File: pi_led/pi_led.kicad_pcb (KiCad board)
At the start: 2 copper layers, 50 x 50 mm, 12 parts, among them CON1 PWR, P1 LED_STRIP, P2 RiPi, Q1 STP16NF06L, Q2 STP16NF06L, Q3 STP16NF06L

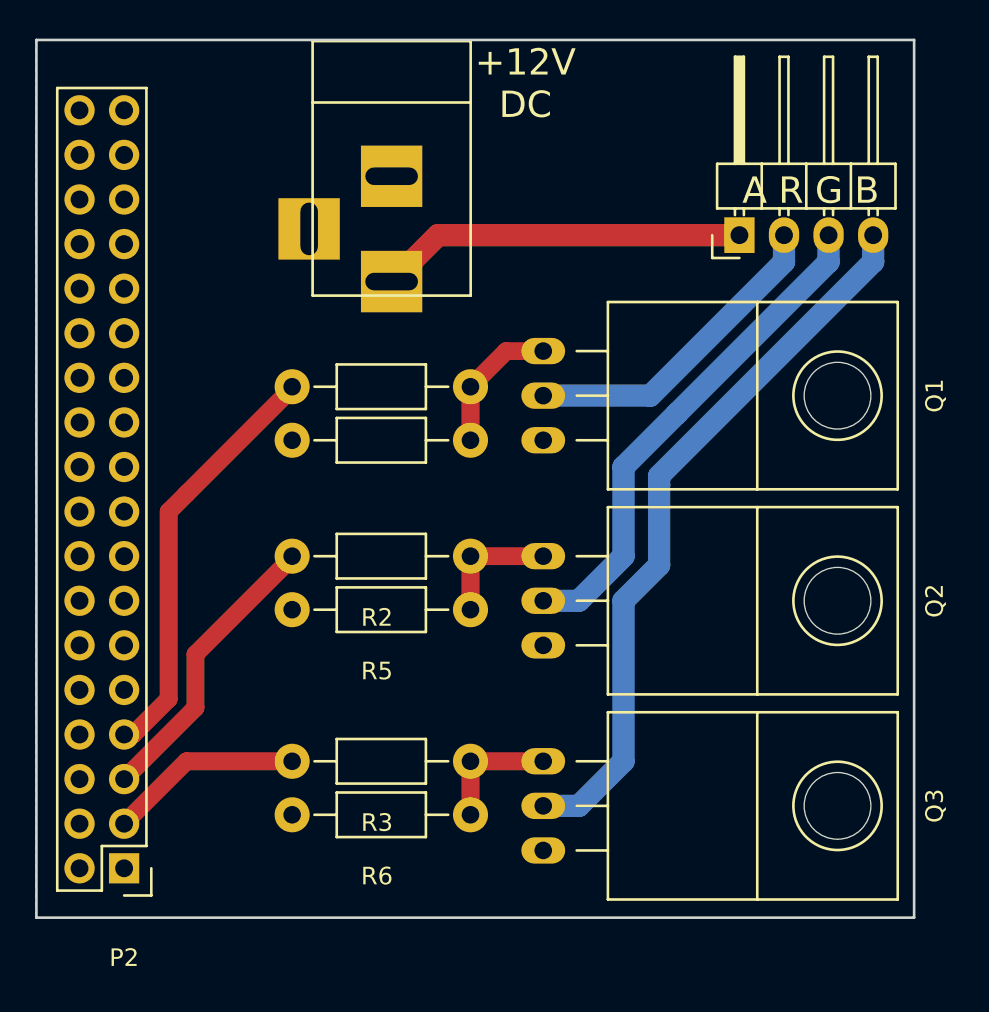
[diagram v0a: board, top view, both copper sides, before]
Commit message: Fix #2, Move labels to silk, General Tidying
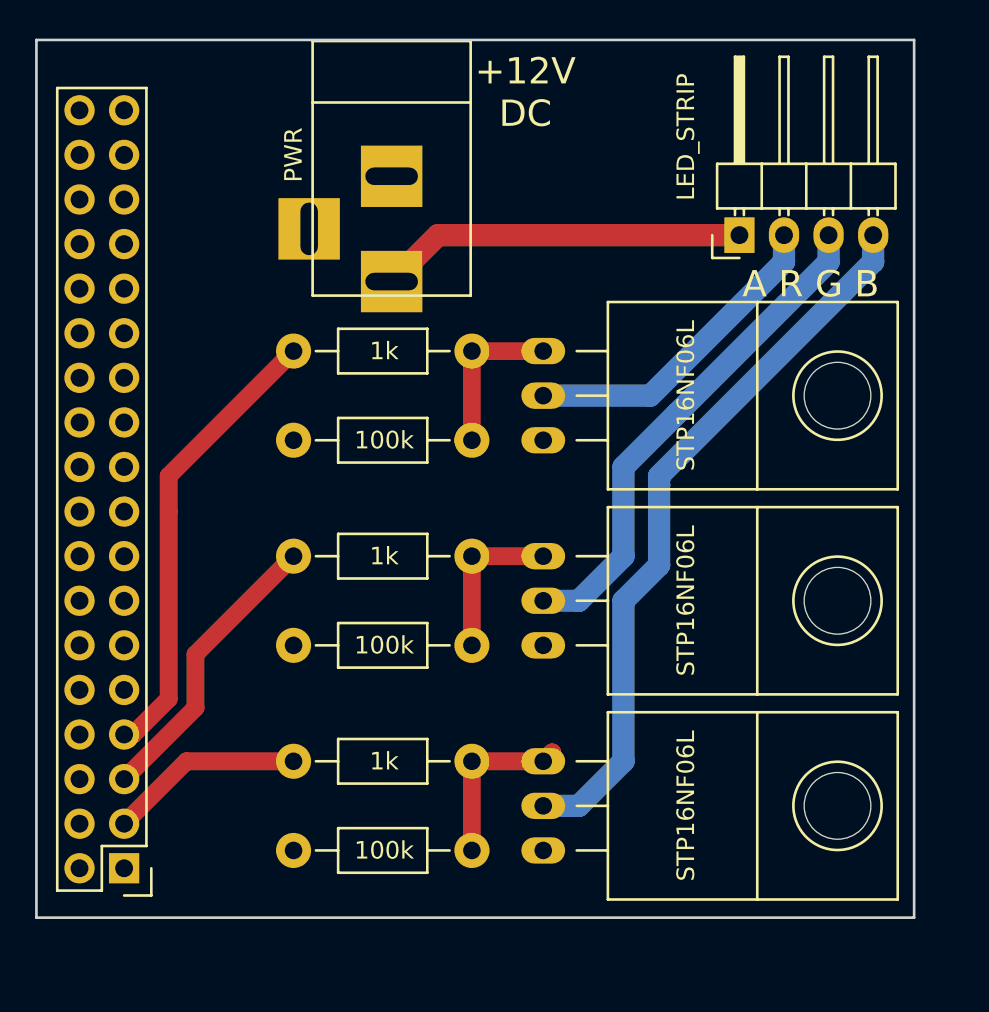
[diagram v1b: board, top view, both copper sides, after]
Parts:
- moved R1 2.03 mm to (109.7, 77.7)
- moved R5 2.03 mm to (109.7, 94.5)
- moved R6 2.03 mm to (109.7, 106.2)
- moved R2 0.08 mm to (109.7, 89.4)
- moved R3 0.08 mm to (109.7, 101.1)
- moved R4 0.08 mm to (109.7, 82.8)
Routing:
- net Net-(Q3-Pad1): track 7.27 -> 11.7 mm
- net Net-(Q2-Pad1): track 7.19 -> 9.73 mm
- net Net-(Q1-Pad1): track 8.03 -> 10.2 mm
- net /GPIO4: track 24.2 -> 26.2 mm

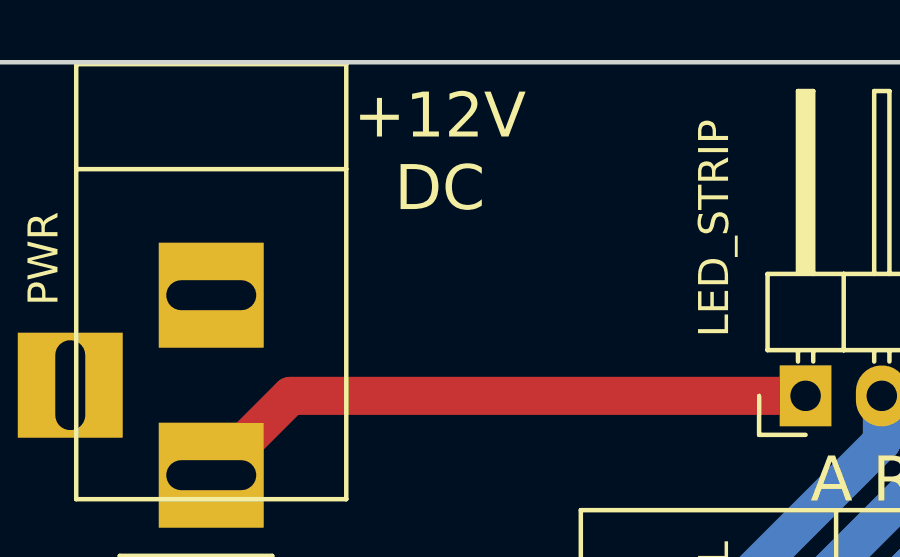
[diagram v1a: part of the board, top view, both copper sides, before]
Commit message: Fix #3: Add centre positive symbol for barrel jack
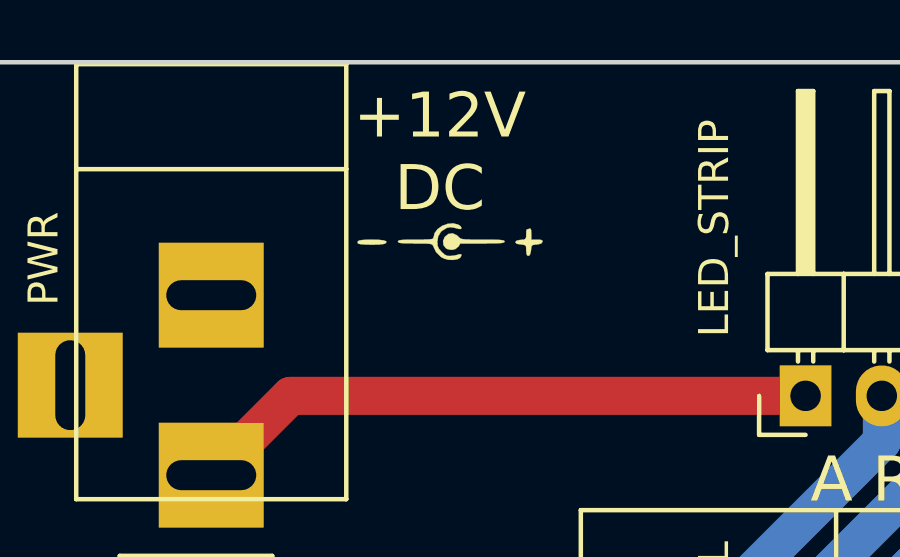
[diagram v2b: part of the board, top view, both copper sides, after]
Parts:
- added G***: LOGO, Hark-Symbols:centre-positive, F.Cu at (118.1, 66.0)
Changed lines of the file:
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@@
-(kicad_pcb (version 4) (host pcbnew "(2015-08-13 BZR 6091)-product")
+(kicad_pcb (version 4) (host pcbnew "(2015-08-15 BZR 6094)-product")
   (general
     (links 21)
     (no_connects 0)
-    (area 89.924999 59.788379 142.1482 113.263)
+    (area 89.924999 59.924999 140.075001 110.075001)
     (thickness 1.6)
     (drawings 7)
     (tracks 48)
     (zones 0)
-    (modules 12)
+    (modules 13)
     (nets 12)
   )
@@
   )
   (setup
-    (last_trace_width 1.016)
+    (last_trace_width 0.25)
     (user_trace_width 0.254)
     (user_trace_width 0.508)
@@
     )
   )
+  (module Hark-Symbols:centre-positive (layer F.Cu)
+    (at 118.11 66.04)
+    (fp_text reference G*** (at 0 0) (layer F.SilkS) hide
+      (effects (font (thickness 0.3)))
+    )
+    (fp_text value LOGO (at 0.75 0) (layer F.SilkS) hide
+      (effects (font (thickness 0.3)))
+    )
+    (fp_poly (pts (xy 0.357841 -0.628205) (xy 0.438038 -0.572657) (xy 0.467372 -0.516128) (xy 0.443939 -0.480281)
+      (xy 0.370416 -0.485314) (xy 0.208621 -0.529296) (xy 0.093957 -0.541113) (xy -0.00408 -0.522383)
+      (xy -0.0441 -0.507268) (xy -0.210808 -0.398613) (xy -0.30937 -0.24002) (xy -0.338667 -0.053558)
+      (xy -0.32788 0.077752) (xy -0.283572 0.177448) (xy -0.190473 0.28366) (xy -0.090635 0.373885)
+      (xy -0.007171 0.413471) (xy 0.097271 0.417214) (xy 0.13761 0.413628) (xy 0.268852 0.394512)
+      (xy 0.373048 0.369479) (xy 0.391583 0.362505) (xy 0.452103 0.354633) (xy 0.465666 0.396148)
+      (xy 0.428608 0.473933) (xy 0.331539 0.525785) (xy 0.195615 0.549858) (xy 0.041994 0.544306)
+      (xy -0.108168 0.507282) (xy -0.209695 0.455083) (xy -0.379057 0.28761) (xy -0.482376 0.074083)
+      (xy -0.500014 0.044045) (xy -0.540088 0.023335) (xy -0.616135 0.01027) (xy -0.741695 0.003167)
+      (xy -0.930305 0.000342) (xy -1.078172 0) (xy -1.312638 -0.001335) (xy -1.474777 -0.00625)
+      (xy -1.576898 -0.01611) (xy -1.631314 -0.032279) (xy -1.650334 -0.056122) (xy -1.651 -0.0635)
+      (xy -1.639137 -0.08911) (xy -1.595459 -0.106951) (xy -1.507838 -0.118323) (xy -1.364141 -0.124525)
+      (xy -1.152241 -0.126858) (xy -1.058334 -0.127) (xy -0.820285 -0.12818) (xy -0.654541 -0.132629)
+      (xy -0.548762 -0.141715) (xy -0.490608 -0.156802) (xy -0.467737 -0.179257) (xy -0.465667 -0.192602)
+      (xy -0.426783 -0.34779) (xy -0.322779 -0.483102) (xy -0.172629 -0.588504) (xy 0.004693 -0.653959)
+      (xy 0.190214 -0.66943) (xy 0.357841 -0.628205)) (layer F.SilkS) (width 0.01))
+    (fp_poly (pts (xy 2.788526 -0.444417) (xy 2.793991 -0.329279) (xy 2.794 -0.322029) (xy 2.794 -0.127)
+      (xy 2.987604 -0.127) (xy 3.106828 -0.121775) (xy 3.160612 -0.100911) (xy 3.167818 -0.056627)
+      (xy 3.167155 -0.052917) (xy 3.128606 0.000697) (xy 3.028397 0.028877) (xy 2.975872 0.034071)
+      (xy 2.863881 0.046678) (xy 2.810816 0.079458) (xy 2.791081 0.157611) (xy 2.785737 0.22128)
+      (xy 2.761837 0.350138) (xy 2.718162 0.413784) (xy 2.661563 0.403147) (xy 2.65377 0.395993)
+      (xy 2.63479 0.338098) (xy 2.62502 0.232245) (xy 2.624666 0.207045) (xy 2.620168 0.106577)
+      (xy 2.590914 0.058397) (xy 2.513264 0.039794) (xy 2.44475 0.034184) (xy 2.318993 0.013535)
+      (xy 2.267282 -0.026998) (xy 2.264833 -0.042333) (xy 2.297559 -0.089086) (xy 2.4018 -0.114879)
+      (xy 2.44475 -0.118851) (xy 2.55744 -0.13085) (xy 2.609287 -0.160751) (xy 2.62392 -0.232183)
+      (xy 2.624666 -0.298768) (xy 2.628651 -0.403958) (xy 2.638588 -0.461807) (xy 2.64237 -0.465667)
+      (xy 2.692133 -0.478836) (xy 2.727037 -0.491363) (xy 2.768426 -0.492838) (xy 2.788526 -0.444417)) (layer F.SilkS) (width 0.01))
+    (fp_poly (pts (xy 0.307928 -0.276933) (xy 0.356125 -0.232833) (xy 0.394055 -0.194419) (xy 0.434666 -0.166647)
+      (xy 0.491385 -0.147789) (xy 0.577638 -0.136121) (xy 0.706854 -0.129918) (xy 0.892459 -0.127453)
+      (xy 1.14788 -0.127001) (xy 1.179604 -0.127) (xy 1.447461 -0.126044) (xy 1.641753 -0.12253)
+      (xy 1.773566 -0.115486) (xy 1.853987 -0.103943) (xy 1.894103 -0.086929) (xy 1.905 -0.0635)
+      (xy 1.894141 -0.040201) (xy 1.854221 -0.023255) (xy 1.774228 -0.011712) (xy 1.643146 -0.004623)
+      (xy 1.449962 -0.001036) (xy 1.183662 -0.000002) (xy 1.169035 0) (xy 0.43307 0)
+      (xy 0.363726 0.105833) (xy 0.266266 0.185437) (xy 0.132597 0.214444) (xy -0.002532 0.188443)
+      (xy -0.053092 0.15875) (xy -0.13562 0.048619) (xy -0.147217 -0.086281) (xy -0.085919 -0.221604)
+      (xy -0.083987 -0.224082) (xy 0.035607 -0.318825) (xy 0.172486 -0.336566) (xy 0.307928 -0.276933)) (layer F.SilkS) (width 0.01))
+    (fp_poly (pts (xy -2.276426 -0.120511) (xy -2.116068 -0.10114) (xy -2.038243 -0.069032) (xy -2.043438 -0.024332)
+      (xy -2.079494 0.004085) (xy -2.148507 0.022074) (xy -2.274279 0.034037) (xy -2.434542 0.040075)
+      (xy -2.607028 0.040287) (xy -2.769471 0.034775) (xy -2.899602 0.023639) (xy -2.975155 0.006979)
+      (xy -2.9845 0) (xy -2.998796 -0.053406) (xy -2.959205 -0.090534) (xy -2.857513 -0.113623)
+      (xy -2.6855 -0.124915) (xy -2.518834 -0.127) (xy -2.276426 -0.120511)) (layer F.SilkS) (width 0.01))
+  )
   (gr_text "A R G B" (at 134.112 73.914) (layer F.SilkS)
     (effects (font (size 1.5 1.5) (thickness 0.3)))
   )
-  (gr_text "Raspberry Pi" (at 98.044 98.044 90) (layer B.SilkS)
+  (gr_text "Raspberry Pi" (at 97.79 86.36 90) (layer B.SilkS)
     (effects (font (size 1.5 1.5) (thickness 0.3)) (justify mirror))
   )
@@
   (segment (start 104.648 77.724) (end 104.568 77.724) (width 1.016) (layer F.Cu) (net 8))
   (segment (start 94.996 99.568) (end 95.504 99.568) (width 1.016) (layer F.Cu) (net 8))
-  (segment (start 114.808 77.724) (end 114.808 82.804) (width 1.016) (layer F.Cu) (net 9) (status C00000))
-  (segment (start 114.808 82.804) (end 114.3 82.804) (width 1.016) (layer F.Cu) (net 9) (status C00000))
-  (segment (start 114.3 82.804) (end 114.808 82.804) (width 1.016) (layer F.Cu) (net 9) (status C00000))
+  (segment (start 114.808 77.724) (end 114.808 82.804) (width 1.016) (layer F.Cu) (net 9))
+  (segment (start 114.808 82.804) (end 114.3 82.804) (width 1.016) (layer F.Cu) (net 9))
+  (segment (start 114.3 82.804) (end 114.808 82.804) (width 1.016) (layer F.Cu) (net 9))
   (segment (start 114.728 77.724) (end 118.872 77.724) (width 1.016) (layer F.Cu) (net 9))
-  (segment (start 114.808 89.408) (end 114.808 94.488) (width 1.016) (layer F.Cu) (net 10) (status C00000))
-  (segment (start 114.808 93.98) (end 114.808 94.488) (width 1.016) (layer F.Cu) (net 10) (status C00000))
+  (segment (start 114.808 89.408) (end 114.808 94.488) (width 1.016) (layer F.Cu) (net 10))
+  (segment (start 114.808 93.98) (end 114.808 94.488) (width 1.016) (layer F.Cu) (net 10))
   (segment (start 114.728 89.408) (end 118.872 89.408) (width 1.016) (layer F.Cu) (net 10))
   (segment (start 114.808 101.092) (end 114.808 106.172) (width 1.016) (layer F.Cu) (net 11))

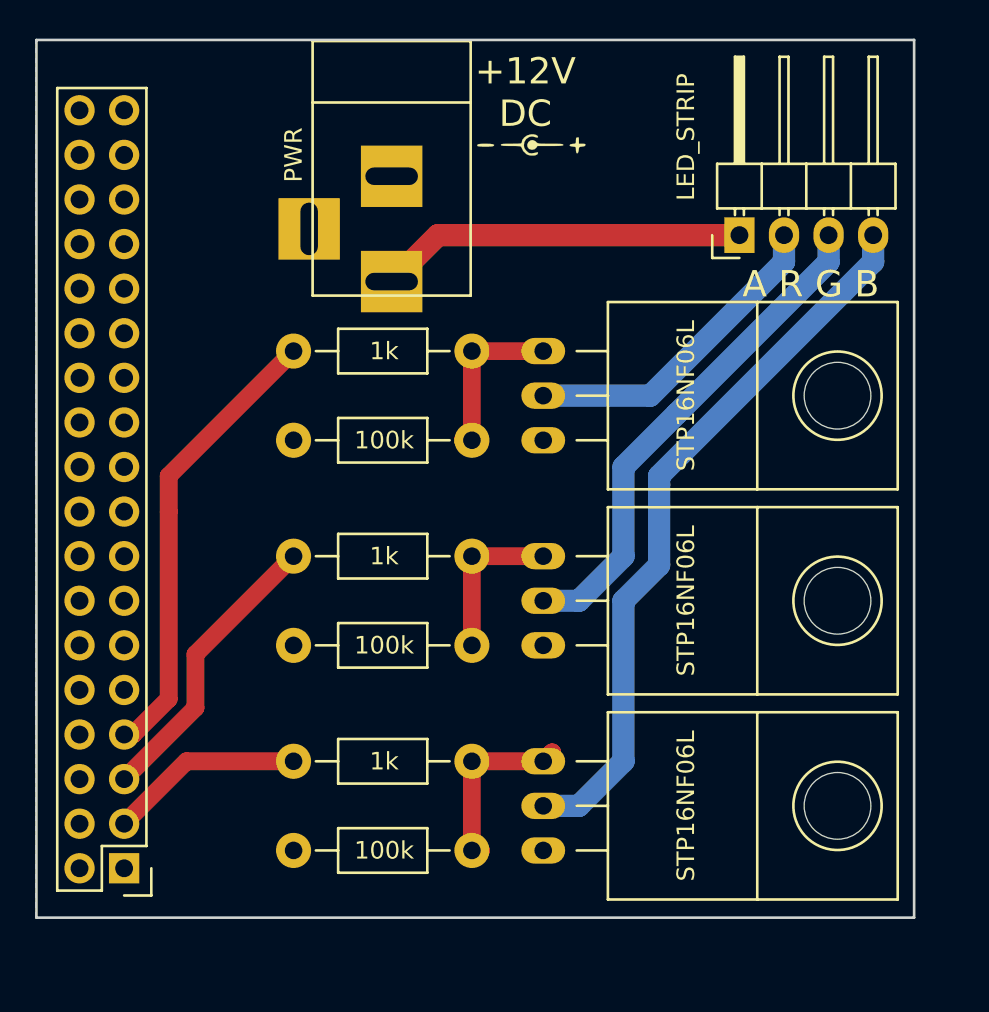
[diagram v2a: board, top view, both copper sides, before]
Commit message: Fix #1: Rounded corners and general prettyfying
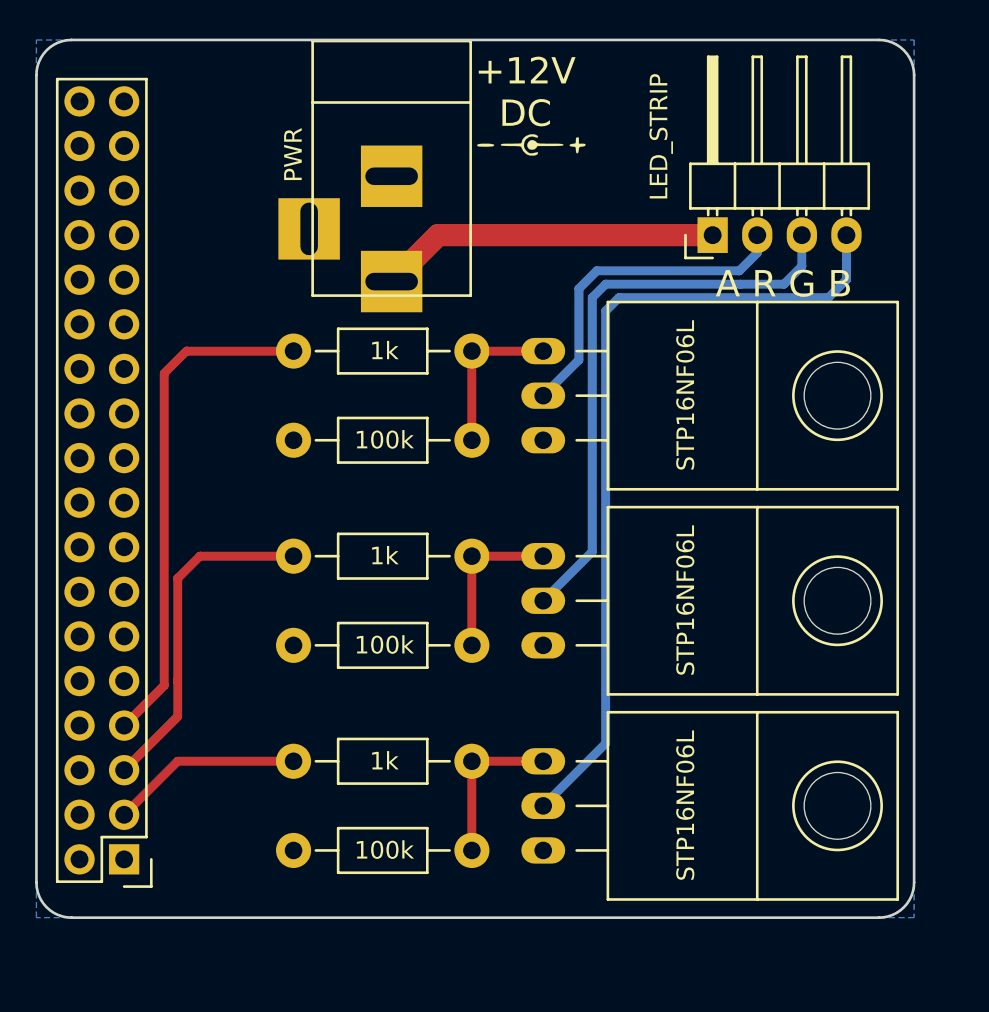
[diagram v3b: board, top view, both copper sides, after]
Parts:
- moved P1 1.52 mm to (128.5, 71.1)
- moved P2 0.51 mm to (95.0, 106.7)
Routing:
- net /LED_B: track 41.5 -> 46.7 mm
- net /LED_G: track 28.8 -> 32.9 mm
- net /GPIO4: track 26.2 -> 28.9 mm
- net /GPIO3: track 16.7 -> 19.3 mm
- net Net-(Q3-Pad1): track 11.7 -> 9.14 mm
- net +12V: track 20.9 -> 19.4 mm
- net Net-(Q1-Pad1): track 10.2 -> 9.14 mm
- net /LED_R: track 18.4 -> 19.0 mm
- net /GPIO2: track 11.5 -> 10.9 mm
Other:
- outline, holes or cut-outs redrawn
